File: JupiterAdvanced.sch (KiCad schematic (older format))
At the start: 233 parts, among them SW1 SW_Push, U1 PRTR5V0U2X, U10 ATmega32U4-AU, Y1 16MHz

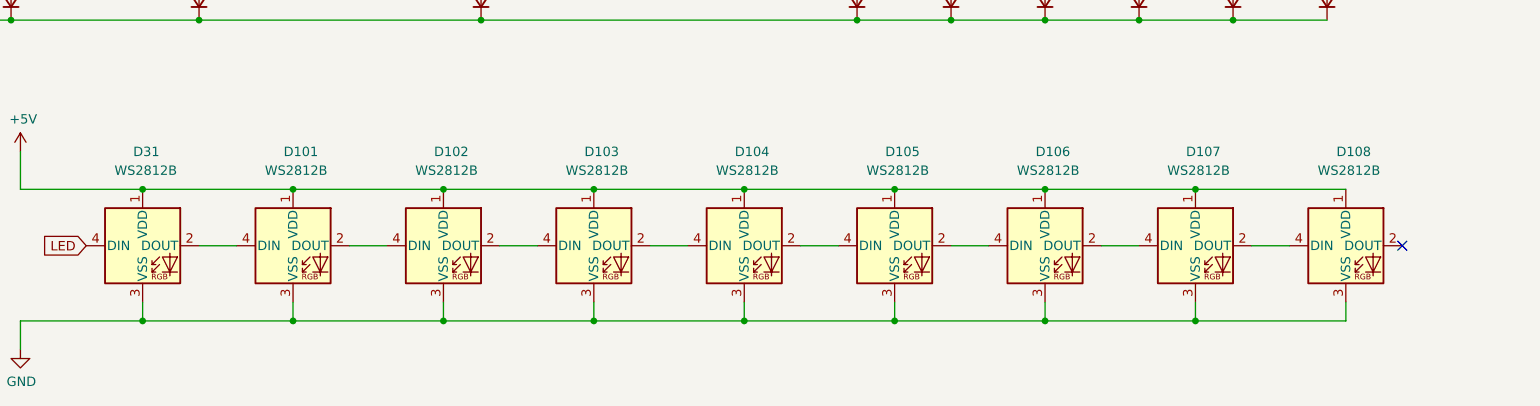
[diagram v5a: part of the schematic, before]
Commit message: Push Switch updated, Underglow LED work started
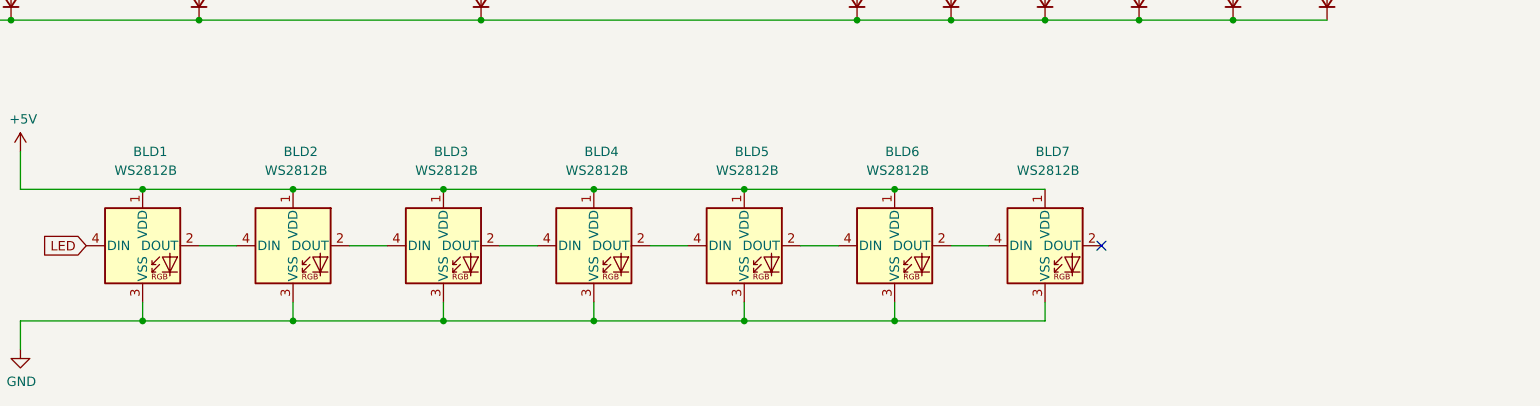
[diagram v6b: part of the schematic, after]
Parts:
- removed D107, D108: WS2812B, LED_SMD:LED_WS2812B_PLCC4_5.0x5.0mm_P3.2mm, symbol LED:WS2812B
- SW1: footprint JupiterAdvancedKbd_localFP:TS-1187A-B-A-B -> Button_Switch_SMD:SW_SPST_SKQG_WithoutStem; LCSC C318884 -> C202424
- renumbered D31 to BLD1, D101 to BLD2, D102 to BLD3, D103 to BLD4, D104 to BLD5, D105 to BLD6, D106 to BLD7
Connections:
- wire segments 444 -> 436
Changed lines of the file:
@@
 F 0 "SW1" H 10650 2385 50  0000 C CNN
 F 1 "SW_Push" H 10650 2294 50  0000 C CNN
-F 2 "JupiterAdvancedKbd_localFP:TS-1187A-B-A-B" H 10650 2300 50  0001 C CNN
+F 2 "Button_Switch_SMD:SW_SPST_SKQG_WithoutStem" H 10650 2300 50  0001 C CNN
 F 3 "~" H 10650 2300 50  0001 C CNN
-F 4 "C318884" H 10650 2100 50  0001 C CNN "LCSC"
+F 4 "C202424" H 10650 2100 50  0001 C CNN "LCSC"
 	1    10650 2100
 	1    0    0    -1
@@
 $EndComp
 $Comp
-L LED:WS2812B D31
+L LED:WS2812B BLD1
 U 1 1 60A403B7
 P 2900 9700
-F 0 "D31" H 2850 10200 50  0000 L CNN
+F 0 "BLD1" H 2850 10200 50  0000 L CNN
 F 1 "WS2812B" H 2750 10100 50  0000 L CNN
 F 2 "LED_SMD:LED_WS2812B_PLCC4_5.0x5.0mm_P3.2mm" H 2950 9400 50  0001 L TNN
@@
 $EndComp
 $Comp
-L LED:WS2812B D101
+L LED:WS2812B BLD2
 U 1 1 60A739C5
 P 3700 9700
-F 0 "D101" H 3650 10200 50  0000 L CNN
+F 0 "BLD2" H 3650 10200 50  0000 L CNN
 F 1 "WS2812B" H 3550 10100 50  0000 L CNN
 F 2 "LED_SMD:LED_WS2812B_PLCC4_5.0x5.0mm_P3.2mm" H 3750 9400 50  0001 L TNN
@@
 $EndComp
 $Comp
-L LED:WS2812B D102
+L LED:WS2812B BLD3
 U 1 1 60A74444
 P 4500 9700
-F 0 "D102" H 4450 10200 50  0000 L CNN
+F 0 "BLD3" H 4450 10200 50  0000 L CNN
 F 1 "WS2812B" H 4350 10100 50  0000 L CNN
 F 2 "LED_SMD:LED_WS2812B_PLCC4_5.0x5.0mm_P3.2mm" H 4550 9400 50  0001 L TNN
@@
 $EndComp
 $Comp
-L LED:WS2812B D103
+L LED:WS2812B BLD4
 U 1 1 60A78CF3
 P 5300 9700
-F 0 "D103" H 5250 10200 50  0000 L CNN
+F 0 "BLD4" H 5250 10200 50  0000 L CNN
 F 1 "WS2812B" H 5150 10100 50  0000 L CNN
 F 2 "LED_SMD:LED_WS2812B_PLCC4_5.0x5.0mm_P3.2mm" H 5350 9400 50  0001 L TNN
@@
 $EndComp
 $Comp
-L LED:WS2812B D104
+L LED:WS2812B BLD5
 U 1 1 60A78CFE
 P 6100 9700
-F 0 "D104" H 6050 10200 50  0000 L CNN
+F 0 "BLD5" H 6050 10200 50  0000 L CNN
 F 1 "WS2812B" H 5950 10100 50  0000 L CNN
 F 2 "LED_SMD:LED_WS2812B_PLCC4_5.0x5.0mm_P3.2mm" H 6150 9400 50  0001 L TNN
@@
 $EndComp
 $Comp
-L LED:WS2812B D105
+L LED:WS2812B BLD6
 U 1 1 60A78D09
 P 6900 9700
-F 0 "D105" H 6850 10200 50  0000 L CNN
+F 0 "BLD6" H 6850 10200 50  0000 L CNN
 F 1 "WS2812B" H 6750 10100 50  0000 L CNN
 F 2 "LED_SMD:LED_WS2812B_PLCC4_5.0x5.0mm_P3.2mm" H 6950 9400 50  0001 L TNN
@@
 $EndComp
 $Comp
-L LED:WS2812B D106
+L LED:WS2812B BLD7
 U 1 1 60AAB8BE
 P 7700 9700
-F 0 "D106" H 7650 10200 50  0000 L CNN
+F 0 "BLD7" H 7650 10200 50  0000 L CNN
 F 1 "WS2812B" H 7550 10100 50  0000 L CNN
 F 2 "LED_SMD:LED_WS2812B_PLCC4_5.0x5.0mm_P3.2mm" H 7750 9400 50  0001 L TNN
@@
 	1    0    0    -1
 $EndComp
-$Comp
-L LED:WS2812B D107
-U 1 1 60AAB8C9
-P 8500 9700
-F 0 "D107" H 8450 10200 50  0000 L CNN
-F 1 "WS2812B" H 8350 10100 50  0000 L CNN
-F 2 "LED_SMD:LED_WS2812B_PLCC4_5.0x5.0mm_P3.2mm" H 8550 9400 50  0001 L TNN
-F 3 "https://cdn-shop.adafruit.com/datasheets/WS2812B.pdf" H 8600 9325 50  0001 L TNN
-F 4 "C114586" H 8500 9700 50  0001 C CNN "LCSC"
-	1    8500 9700
-	1    0    0    -1
-$EndComp
-$Comp
-L LED:WS2812B D108
-U 1 1 60AAB8D4
-P 9300 9700
-F 0 "D108" H 9250 10200 50  0000 L CNN
-F 1 "WS2812B" H 9150 10100 50  0000 L CNN
-F 2 "LED_SMD:LED_WS2812B_PLCC4_5.0x5.0mm_P3.2mm" H 9350 9400 50  0001 L TNN
-F 3 "https://cdn-shop.adafruit.com/datasheets/WS2812B.pdf" H 9400 9325 50  0001 L TNN
-F 4 "C114586" H 9300 9700 50  0001 C CNN "LCSC"
-	1    9300 9700
-	1    0    0    -1
-$EndComp
-Wire Wire Line
-	9300 10000 9300 10100
-Wire Wire Line
-	9300 10100 8500 10100
 Wire Wire Line
 	2250 10100 2250 10250
@@
 Wire Wire Line
 	7700 10000 7700 10100
-Connection ~ 7700 10100
 Wire Wire Line
 	7700 10100 6900 10100
-Wire Wire Line
-	8500 10000 8500 10100
-Connection ~ 8500 10100
-Wire Wire Line
-	8500 10100 7700 10100
 $Comp
 L power:GND #PWR0118
@@
 $EndComp
 Wire Wire Line
-	9300 9400 8500 9400
-Wire Wire Line
 	2250 9400 2250 9200
 Connection ~ 2900 9400
@@
 Wire Wire Line
 	6900 9400 6100 9400
-Connection ~ 7700 9400
 Wire Wire Line
 	7700 9400 6900 9400
-Connection ~ 8500 9400
-Wire Wire Line
-	8500 9400 7700 9400
 $Comp
 L power:+5V #PWR0119
@@
 Wire Wire Line
 	7200 9700 7400 9700
-Wire Wire Line
-	8000 9700 8200 9700
-Wire Wire Line
-	8800 9700 9000 9700
-NoConn ~ 9600 9700
 Text GLabel 12300 4550 2    50   Input ~ 0
 LED
+NoConn ~ 8000 9700
 $EndSCHEMATC
